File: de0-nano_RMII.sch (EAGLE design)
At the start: 49 parts, among them IC2 AD5683, U1 DP83848, X1 1-227161-2

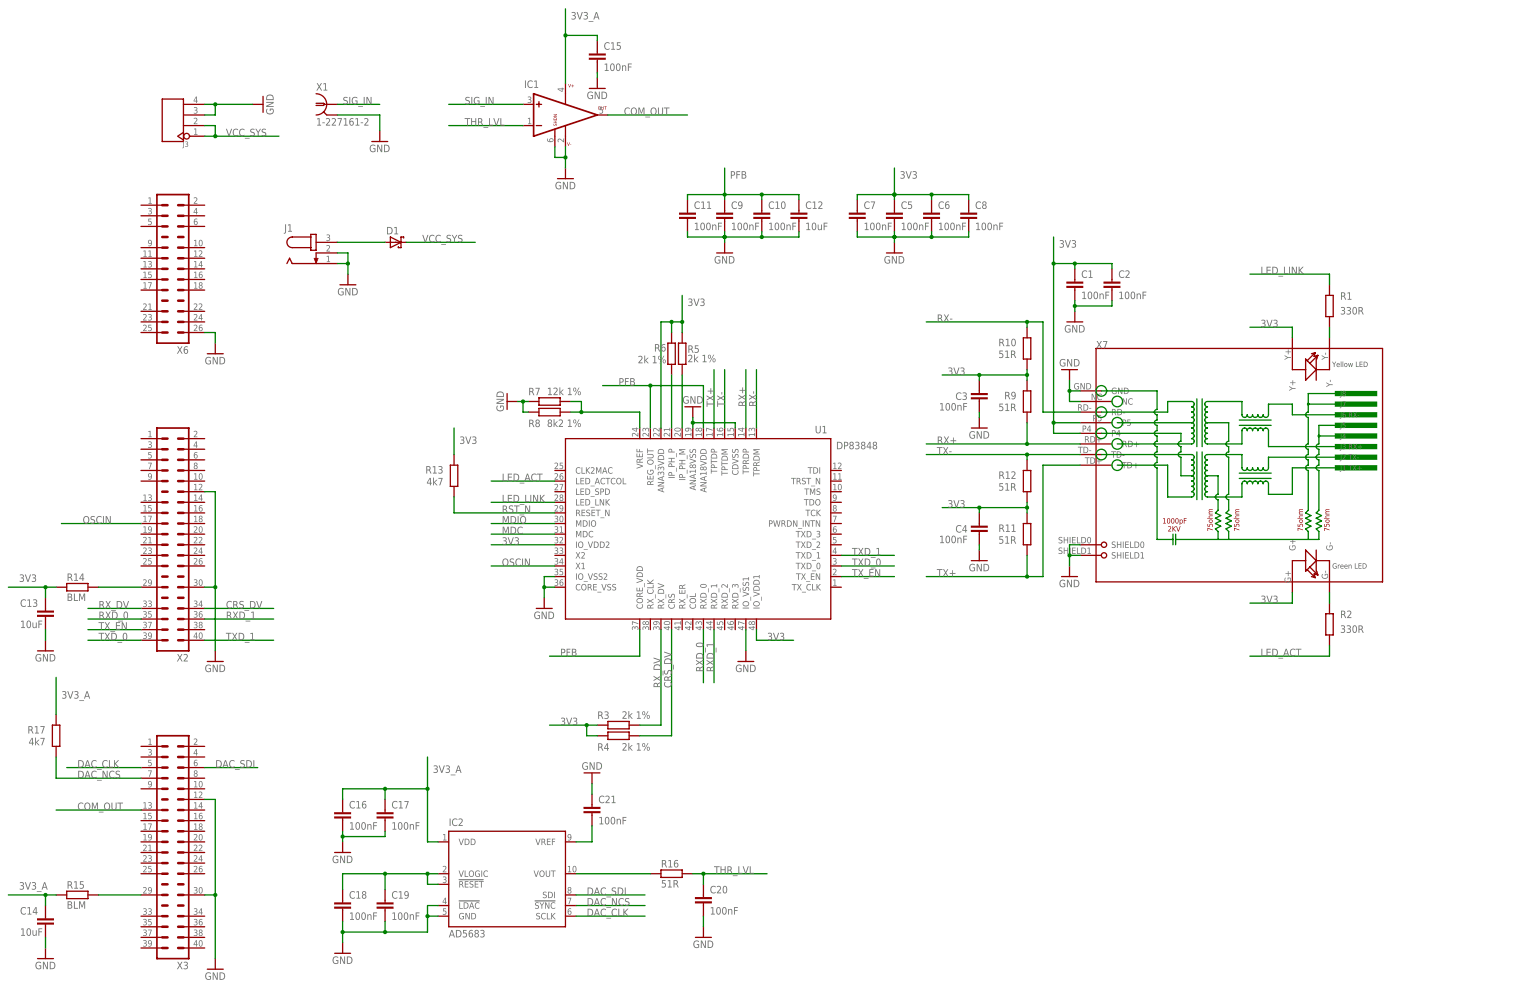
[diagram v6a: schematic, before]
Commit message: added protection diodes at the input, and separate crystal oscillator
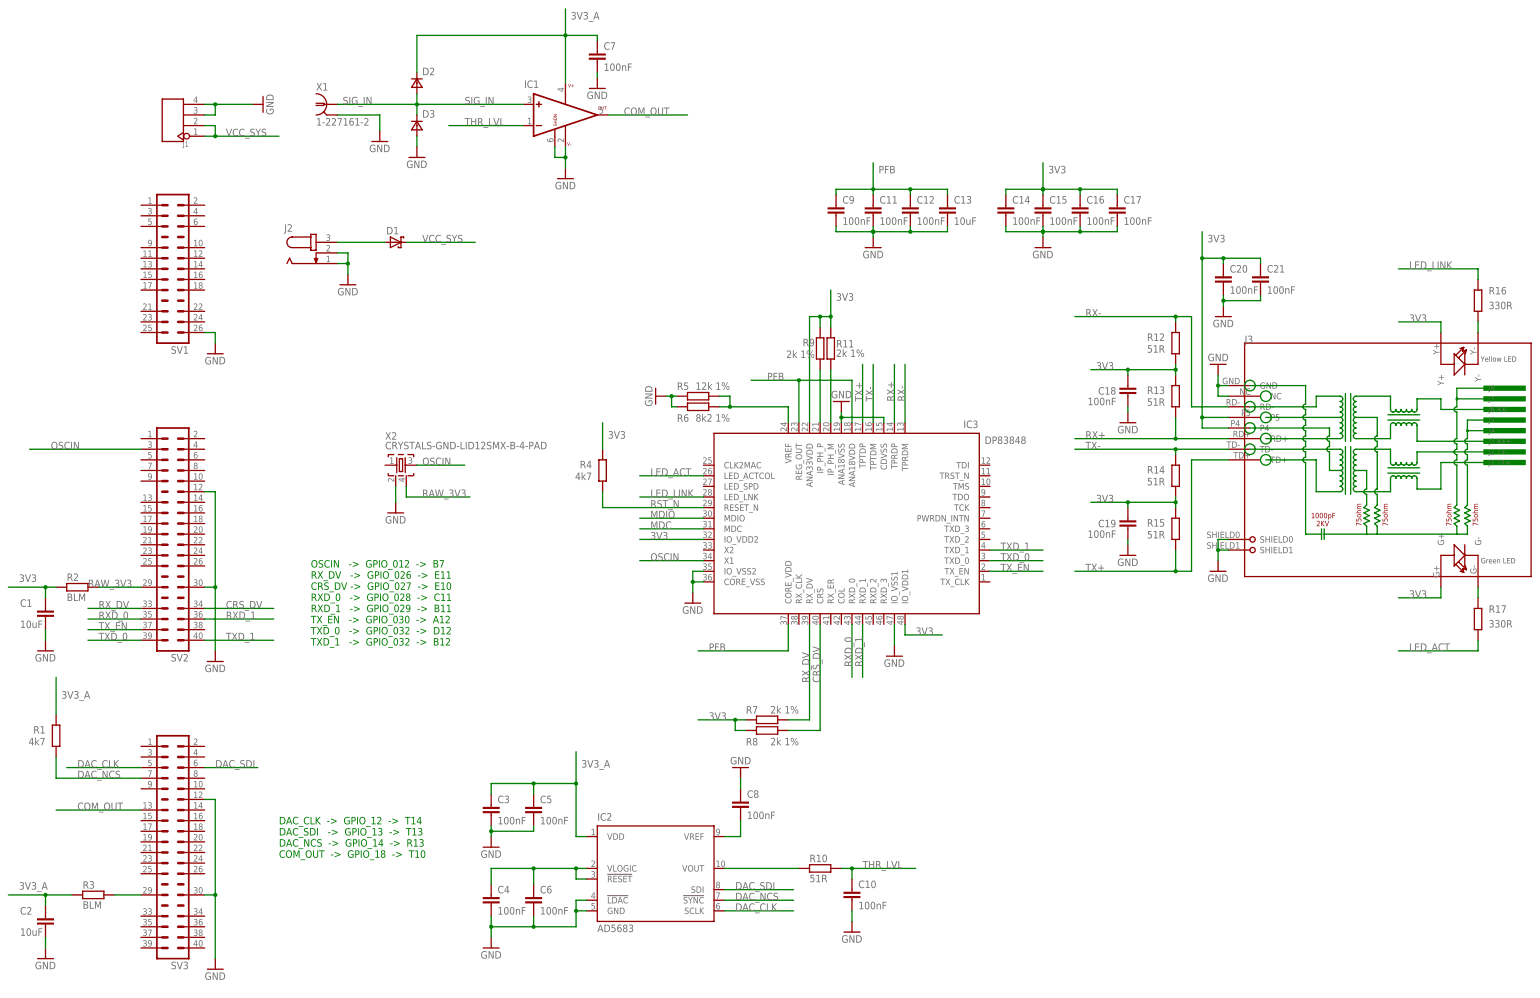
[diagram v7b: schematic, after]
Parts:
- removed U1: DP83848, national-semiconductor:DP83848
- removed X7: (no value), seeed_connector:RJ45-HR911105A-HR911105A
- added D2, D3: (no value), zetex:DSOD323
- added IC3: DP83848, national-semiconductor:DP83848
- added J2: (no value), con-jack:JACK-PLUG1
- added SV2: (no value), con-lstb:MA20-2_ALT
- C1, C2: value 100nF -> 10uF; device resistor:C-EUC0603 -> resistor:C-EUC0805
- C12, C14: value 10uF -> 100nF; device resistor:C-EUC0805 -> resistor:C-EUC0603
- J1: device con-jack:JACK-PLUG1 -> seeed_connector:HEADER-4P-60/35MIL
- J3: device seeed_connector:HEADER-4P-60/35MIL -> seeed_connector:RJ45-HR911105A-HR911105A
- R1: value 330R -> 4k7
- R11, R9: value 51R -> 2k 1%
- R13: value 4k7 -> 51R
- R14, R15: value BLM -> 51R
- R16: value 51R -> 330R
- R17: value 4k7 -> 330R
- R2: value 330R -> BLM
- R3: value 2k 1% -> BLM
- R4: value 2k 1% -> 4k7
- R5: value 2k 1% -> 12k 1%
- R6: value 2k 1% -> 8k2 1%
- R7: value 12k 1% -> 2k 1%
- R8: value 8k2 1% -> 2k 1%
- X2: value (none) -> CRYSTALS-GND-LID12SMX-B-4-PAD; device con-lstb:MA20-2_ALT -> IQD-Frequency-Products:CRYSTALS-GND-LID12SMX-B-4-PAD
- renumbered X3 to SV3, X6 to SV1
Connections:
- removed net N$7: R14.2, X2.29
- new net RAW_3V3: R2.2, SV2.29, X2.4
- net 3V3: now also C14.1, C15.1, C16.1, C17.1, C18.1, C19.1, C20.1, C21.1, IC3.ANA33VDD, IC3.IO_VDD1, IC3.IO_VDD2, J3.G+, J3.P4, J3.P5, J3.Y+, R11.2, R14.2, R15.1, R2.1, R4.1, R7.2, R8.2, R9.2; no longer C13.1, C2.1, C3.1, C4.1, C5.1, C6.1, C7.1, C8.1, R10.2, R11.1, R14.1, R3.2, R4.2, R5.2, R6.2, R9.1, U1.ANA33VDD, U1.IO_VDD1, U1.IO_VDD2, X7.G+, X7.P4, X7.P5, X7.Y+
- net 3V3_A: now also C2.1, C3.1, C5.1, C7.1, D2.C, R1.1, R3.1; no longer C14.1, C15.1, C16.1, C17.1, R15.1, R17.1
- net CRS_DV: now also IC3.CRS, R8.1, SV2.34; no longer R4.1, U1.CRS, X2.34
- net DAC_NCS: now also R1.2; no longer R17.2
- net GND: now also D3.A, IC3.ANA18VSS, IC3.CDVSS, IC3.CORE_VSS, IC3.IO_VSS1, IC3.IO_VSS2, J1.P$3, J1.P$4, J2.1, J2.2, J3.GND, J3.NC, J3.SHIELD0, J3.SHIELD1, R5.2, R6.2, SV2.12, SV2.30, X2.2; no longer J1.1, J1.2, J3.P$3, J3.P$4, R7.2, R8.2, U1.ANA18VSS, U1.CDVSS, U1.CORE_VSS, U1.IO_VSS1, U1.IO_VSS2, X2.12, X2.30, X7.GND, X7.NC, X7.SHIELD0, X7.SHIELD1
- net LED_ACT: now also IC3.LED_ACTCOL, R17.1; no longer R2.1, U1.LED_ACTCOL
- net LED_LINK: now also IC3.LED_LNK, R16.2; no longer R1.2, U1.LED_LNK
- net MDC: now also IC3.MDC; no longer U1.MDC
- net MDIO: now also IC3.MDIO; no longer U1.MDIO
- net N$1: now also R3.2; no longer R15.2
- net N$13: now also C8.1; no longer C21.1
- net N$3: now also IC3.IP_PH_P, R9.1; no longer R6.1, U1.IP_PH_P
- net N$4: now also J3.Y-, R16.1; no longer R1.1, X7.Y-
- net N$5: now also IC3.IP_PH_M, R11.1; no longer R5.1, U1.IP_PH_M
- net N$6: now also J3.G-, R17.2; no longer R2.2, X7.G-
- net N$8: now also R10.1; no longer R16.1
- net N$9: now also IC3.VREF, R5.1, R6.1; no longer R7.1, R8.1, U1.VREF
- net OSCIN: now also IC3.X1, SV2.3, X2.3; no longer U1.X1, X2.17
- net PFB: now also C13.1, IC3.ANA18VDD, IC3.CORE_VDD, IC3.REG_OUT; no longer C10.1, U1.ANA18VDD, U1.CORE_VDD, U1.REG_OUT
- net RST_N: now also IC3.RESET_N, R4.2; no longer R13.2, U1.RESET_N
- net RX+: now also IC3.TPRDP, J3.RD+, R13.2; no longer R9.2, U1.TPRDP, X7.RD+
- net RX-: now also IC3.TPRDM, J3.RD-, R12.1; no longer R10.1, U1.TPRDM, X7.RD-
- net RXD_0: now also IC3.RXD_0, SV2.35; no longer U1.RXD_0, X2.35
- net RXD_1: now also IC3.RXD_1, SV2.36; no longer U1.RXD_1, X2.36
- net RX_DV: now also IC3.RX_DV, R7.1, SV2.33; no longer R3.1, U1.RX_DV, X2.33
- net SIG_IN: now also D2.A, D3.C
- net THR_LVL: now also C10.1, R10.2; no longer C20.1, R16.2
- net TX+: now also IC3.TPTDP, J3.TD+, R15.2; no longer R11.2, U1.TPTDP, X7.TD+
- net TX-: now also IC3.TPTDM, J3.TD-, R14.1; no longer R12.1, U1.TPTDM, X7.TD-
- net TXD_0: now also IC3.TXD_0, SV2.39; no longer U1.TXD_0, X2.39
- net TXD_1: now also IC3.TXD_1, SV2.40; no longer U1.TXD_1, X2.40
- net TX_EN: now also IC3.TX_EN, SV2.37; no longer U1.TX_EN, X2.37
- net VCC_SYS: now also J1.P$1, J1.P$2; no longer J3.P$1, J3.P$2
- net VLOGIC: now also C4.1, C6.1; no longer C18.1, C19.1
- net V_RAW: now also J2.3; no longer J1.3
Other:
- note added: "DAC_CLK -> GPIO_12 -> T14 DAC_SDI -> GPIO_13 -> T13 DAC_NCS -> GPIO_14 -> R13 COM_OUT -> GPIO_18 -> T10"
- note added: "OSCIN -> GPIO_012 -> B7 RX_DV -> GPIO_026 -> E11 CRS_DV -> GPIO_027 -> E10 RXD_0 -> GPIO_028 -> C11 RXD_1 -> GPIO_029 -> B11 TX_EN -> GPIO_030 -> A12 TXD_0 -> GPIO_032 -> D12 TXD_1 -> GPIO_032 -> B12"
- moved on the sheet: C1, C10, C11, C12, C13, C14, C15, C16, C17, C18, C19, C2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

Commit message: gerber generated
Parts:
- C13: value 10uF -> 100nF; device resistor:C-EUC0805 -> resistor:C-EUC0603
- C7: value 100nF -> 10uF; device resistor:C-EUC0603 -> resistor:C-EUC0805
- IC1: value (none) -> DP83848; device linear-technology:LT1719 -> national-semiconductor:DP83848
- IC2: value AD5683 -> (none); device analog-devices:AD5683 -> linear-technology:LT1719
- IC3: value DP83848 -> AD5683; device national-semiconductor:DP83848 -> analog-devices:AD5683
- J1: device seeed_connector:HEADER-4P-60/35MIL -> con-jack:JACK-PLUG1
- J2: device con-jack:JACK-PLUG1 -> seeed_connector:HEADER-4P-60/35MIL
- R10: value 51R -> 2k 1%
- R11: value 2k 1% -> 51R
- X1: value 1-227161-2 -> CRYSTALS-GND-LID12SMX-B-4-PAD; device con-coax:1-227161-2 -> IQD-Frequency-Products:CRYSTALS-GND-LID12SMX-B-4-PAD
- X2: value CRYSTALS-GND-LID12SMX-B-4-PAD -> 1-227161-2; device IQD-Frequency-Products:CRYSTALS-GND-LID12SMX-B-4-PAD -> con-coax:1-227161-2
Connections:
- net 3V3: now also C10.1, C13.1, C8.1, C9.1, IC1.ANA33VDD, IC1.IO_VDD1, IC1.IO_VDD2, R10.2, R12.1, R13.2, R14.1; no longer C16.1, C17.1, C20.1, C21.1, IC3.ANA33VDD, IC3.IO_VDD1, IC3.IO_VDD2, R12.2, R13.1, R14.2, R15.1
- net 3V3_A: now also C11.1, C16.1, IC2.V+, IC3.VDD; no longer C3.1, C7.1, IC1.V+, IC2.VDD
- net COM_OUT: now also IC2.OUT; no longer IC1.OUT
- net CRS_DV: now also IC1.CRS; no longer IC3.CRS
- net DAC_CLK: now also IC3.SCLK; no longer IC2.SCLK
- net DAC_NCS: now also IC3.!SYNC; no longer IC2.!SYNC
- net DAC_SDI: now also IC3.SDI; no longer IC2.SDI
- net GND: now also IC1.ANA18VSS, IC1.CDVSS, IC1.CORE_VSS, IC1.IO_VSS1, IC1.IO_VSS2, IC2.SHDN, IC2.V-, IC3.!LDAC, IC3.GND, J1.1, J1.2, J2.P$3, J2.P$4; no longer IC1.SHDN, IC1.V-, IC2.!LDAC, IC2.GND, IC3.ANA18VSS, IC3.CDVSS, IC3.CORE_VSS, IC3.IO_VSS1, IC3.IO_VSS2, J1.P$3, J1.P$4, J2.1, J2.2
- net LED_ACT: now also IC1.LED_ACTCOL; no longer IC3.LED_ACTCOL
- net LED_LINK: now also IC1.LED_LNK; no longer IC3.LED_LNK
- net MDC: now also IC1.MDC; no longer IC3.MDC
- net MDIO: now also IC1.MDIO; no longer IC3.MDIO
- net N$13: now also C20.1, IC3.VREF; no longer C8.1, IC2.VREF
- net N$3: now also IC1.IP_PH_P; no longer IC3.IP_PH_P
- net N$5: now also IC1.IP_PH_M, R10.1; no longer IC3.IP_PH_M, R11.1
- net N$8: now also IC3.VOUT, R15.1; no longer IC2.VOUT, R10.1
- net N$9: now also IC1.VREF; no longer IC3.VREF
- net OSCIN: now also IC1.X1, X1.3; no longer IC3.X1, X2.3
- net PFB: now also C3.1, C4.1, C6.1, C7.1, IC1.ANA18VDD, IC1.CORE_VDD, IC1.REG_OUT; no longer C11.1, C12.1, C13.1, C9.1, IC3.ANA18VDD, IC3.CORE_VDD, IC3.REG_OUT
- net RAW_3V3: now also X1.4; no longer X2.4
- net RST_N: now also IC1.RESET_N; no longer IC3.RESET_N
- net RX+: now also IC1.TPRDP, R12.2; no longer IC3.TPRDP, R13.2
- net RX-: now also IC1.TPRDM, R11.1; no longer IC3.TPRDM, R12.1
- net RXD_0: now also IC1.RXD_0; no longer IC3.RXD_0
- net RXD_1: now also IC1.RXD_1; no longer IC3.RXD_1
- net RX_DV: now also IC1.RX_DV; no longer IC3.RX_DV
- net SIG_IN: now also IC2.+IN, X2.1; no longer IC1.+IN, X1.1
- net THR_LVL: now also C21.1, IC2.-IN, R15.2; no longer C10.1, IC1.-IN, R10.2
- net TX+: now also IC1.TPTDP, R14.2; no longer IC3.TPTDP, R15.2
- net TX-: now also IC1.TPTDM, R13.1; no longer IC3.TPTDM, R14.1
- net TXD_0: now also IC1.TXD_0; no longer IC3.TXD_0
- net TXD_1: now also IC1.TXD_1; no longer IC3.TXD_1
- net TX_EN: now also IC1.TX_EN; no longer IC3.TX_EN
- net VCC_SYS: now also J2.P$1, J2.P$2; no longer J1.P$1, J1.P$2
- net VLOGIC: now also C12.1, C17.1, IC3.!RESET, IC3.VLOGIC; no longer C4.1, C6.1, IC2.!RESET, IC2.VLOGIC
- net V_RAW: now also J1.3; no longer J2.3
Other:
- note added: "OSCIN -> GPIO_0_IN1 -> B8 RX_DV -> GPIO_026 -> E11 CRS_DV -> GPIO_027 -> E10 RXD_0 -> GPIO_028 -> C11 RXD_1 -> GPIO_029 -> B11 TX_EN -> GPIO_030 -> A12 TXD_0 -> GPIO_032 -> D12 TXD_1 -> GPIO_032 -> B12"
- note removed: "OSCIN -> GPIO_012 -> B7 RX_DV -> GPIO_026 -> E11 CRS_DV -> GPIO_027 -> E10 RXD_0 -> GPIO_028 -> C11 RXD_1 -> GPIO_029 -> B11 TX_EN -> GPIO_030 -> A12 TXD_0 -> GPIO_032 -> D12 TXD_1 -> GPIO_032 -> B12"
- moved on the sheet: C10, C11, C12, C13, C14, C15, C16, C17, C18, C19, C20, C21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
